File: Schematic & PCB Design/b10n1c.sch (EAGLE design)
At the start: 26 parts, among them U1 nRF8001, Y1 16MHz, Y2 FC-255 32.7680K-A3

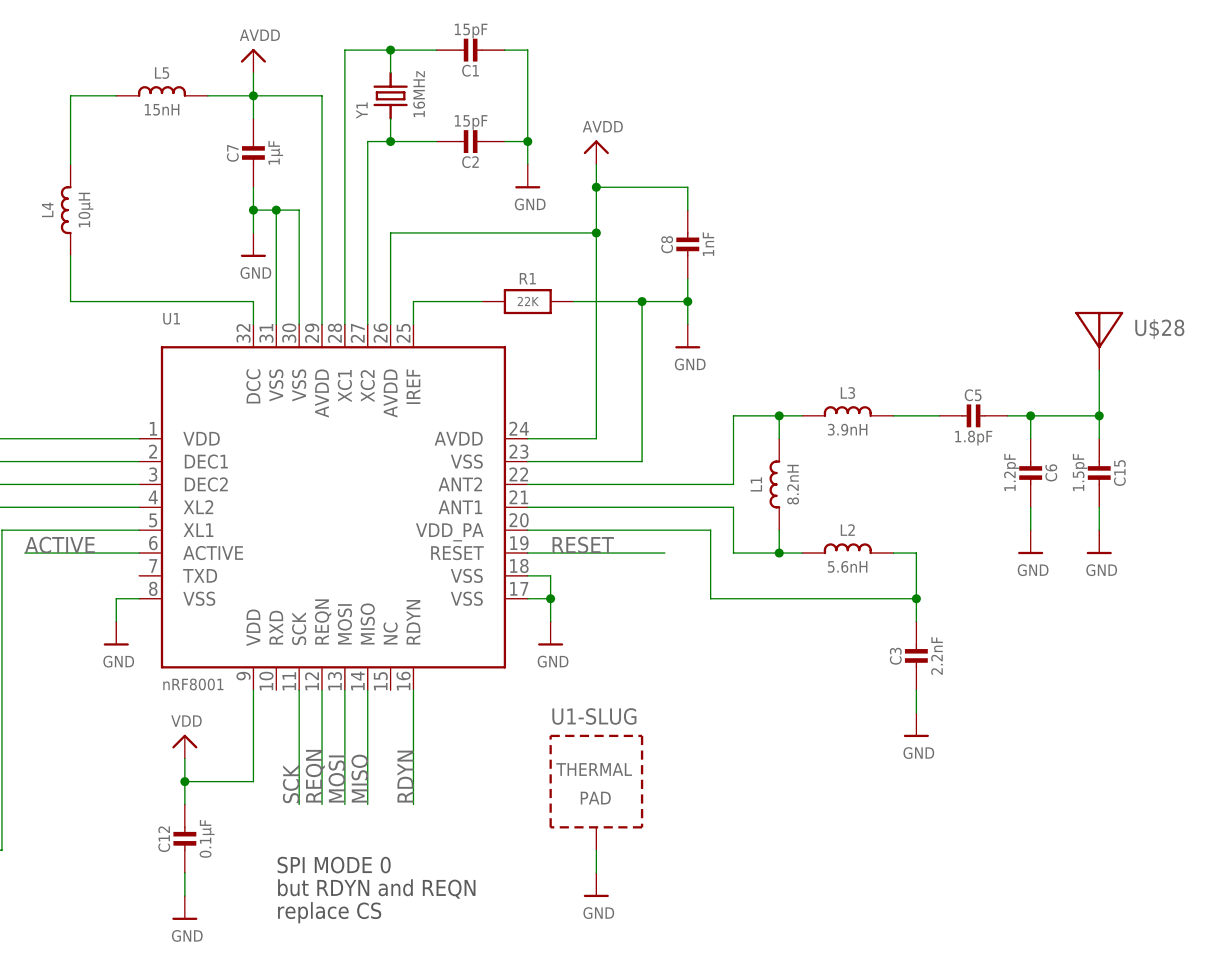
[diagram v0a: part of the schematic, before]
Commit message: Improvement for NRF8001 circuit
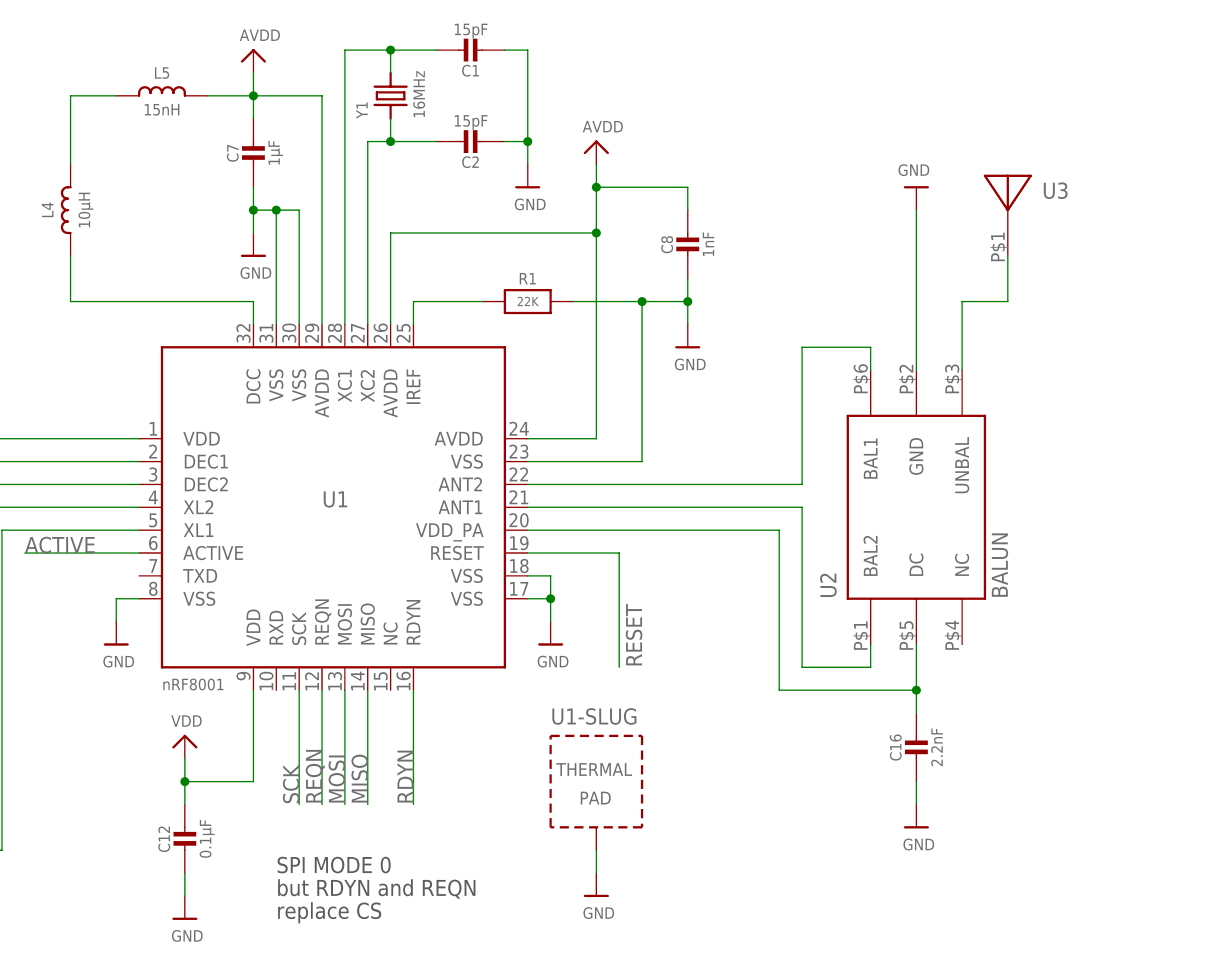
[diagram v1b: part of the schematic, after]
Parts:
- removed C15: 1.5pF, microbuilder:CAP_CERAMIC_0402MP
- removed C3: 2.2nF, microbuilder:CAP_CERAMIC_0402
- removed C5: 1.8pF, microbuilder:CAP_CERAMIC_0402MP
- removed C6: 1.2pF, microbuilder:CAP_CERAMIC_0402MP
- removed L1: 8.2nH, microbuilder:INDUCTOR_0402
- removed L2: 5.6nH, microbuilder:INDUCTOR_0402
- removed L3: 3.9nH, microbuilder:INDUCTOR_0402
- removed U$28: (no value), microbuilder:ANTENNA_PCBNRF8001_1.6MM
- added C16: 2.2nF, microbuilder:CAP_CERAMIC_0402
- added U2: 2450BM14A0002T, baluns:2450BM14A0002T
- added U3: 2450AT18A100, Johanson_antenna:2450AT18A100
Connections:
- removed net N$13: C15.2, C5.1, C6.2, U$28.P$1
- removed net N$2: L1.2, L3.1, U1A.ANT2
- removed net N$3: L1.1, L2.1, U1A.ANT1
- removed net N$4: C3.1, L2.2, U1A.VDD_PA
- removed net N$6: C5.2, L3.2
- new net N$1: C16.1, U1A.VDD_PA, U2.DC
- new net N$14: U1A.ANT1, U2.BAL2
- new net N$15: U1A.ANT2, U2.BAL1
- new net N$16: U2.UNBAL, U3.P$1
- net GND: now also C16.2, U2.GND; no longer C15.1, C3.2, C6.1
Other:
- note added: "BALUN"

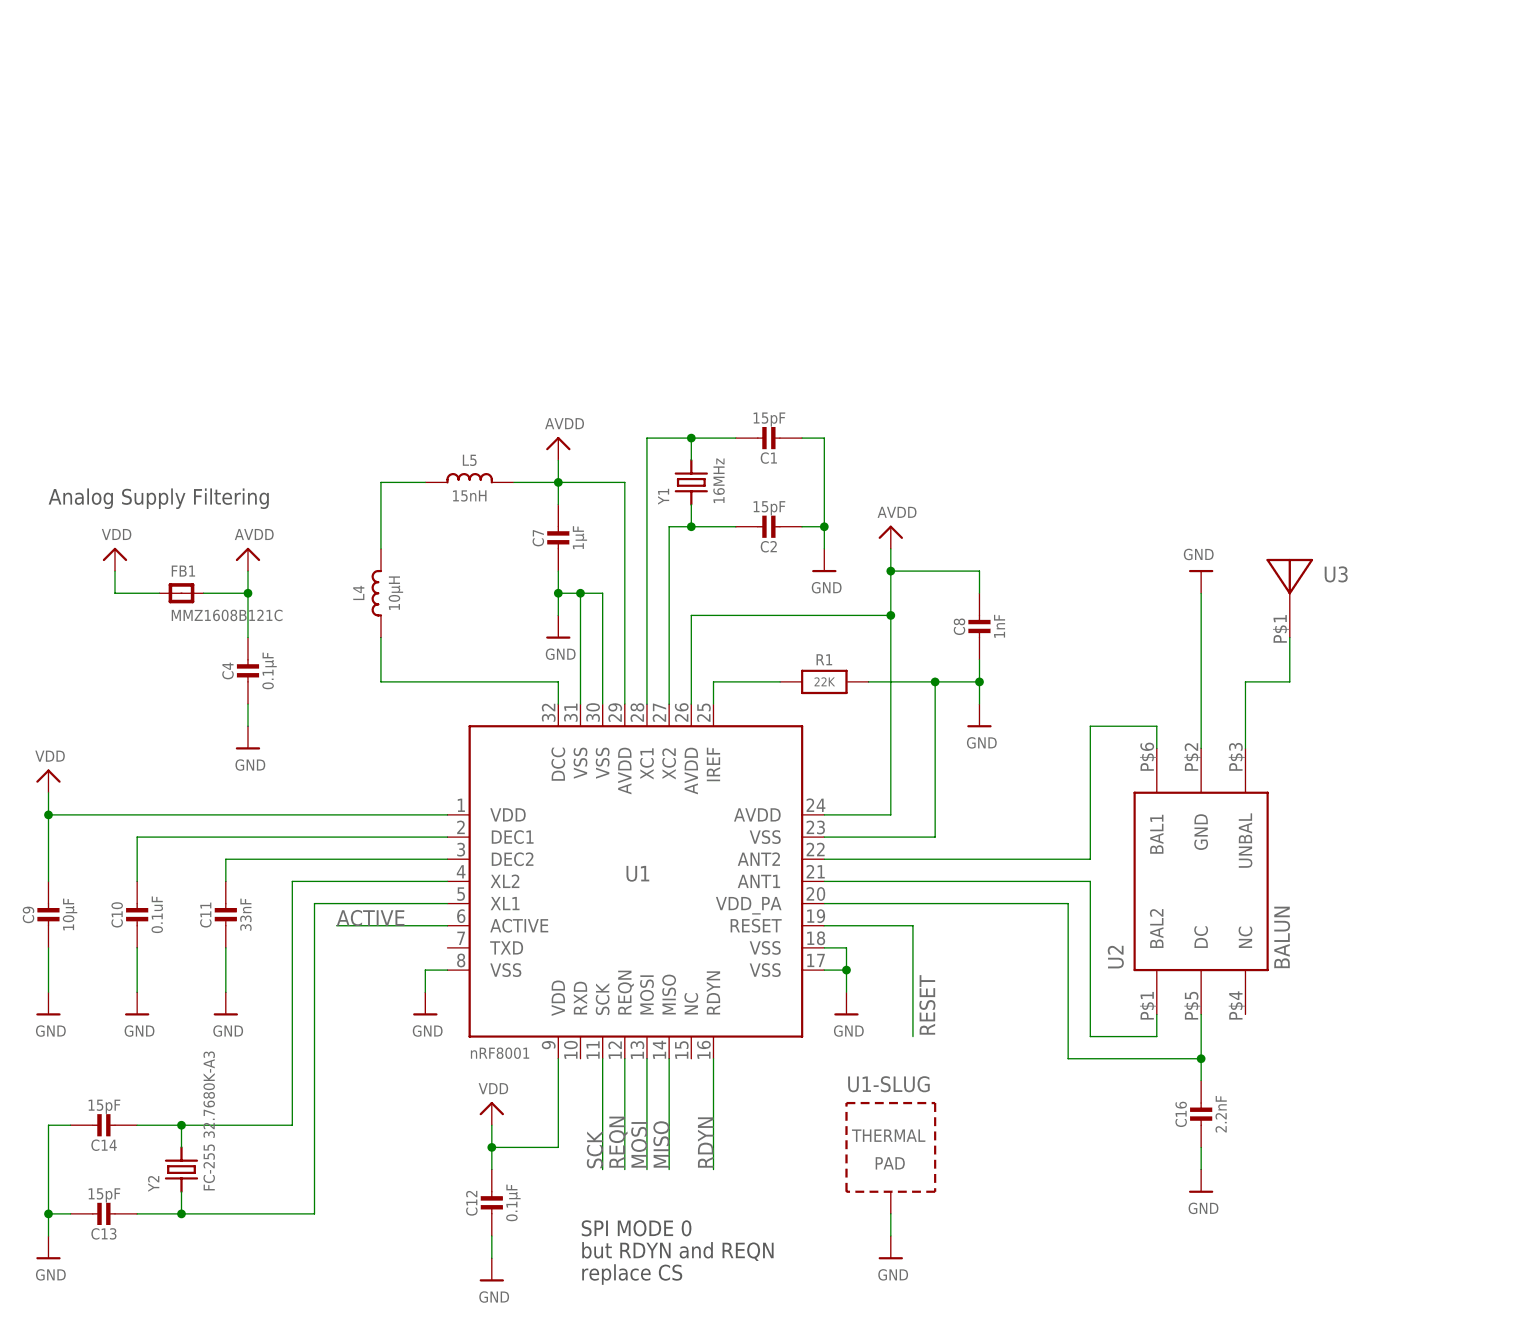
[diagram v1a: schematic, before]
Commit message: NRF8001 schem+layout completed
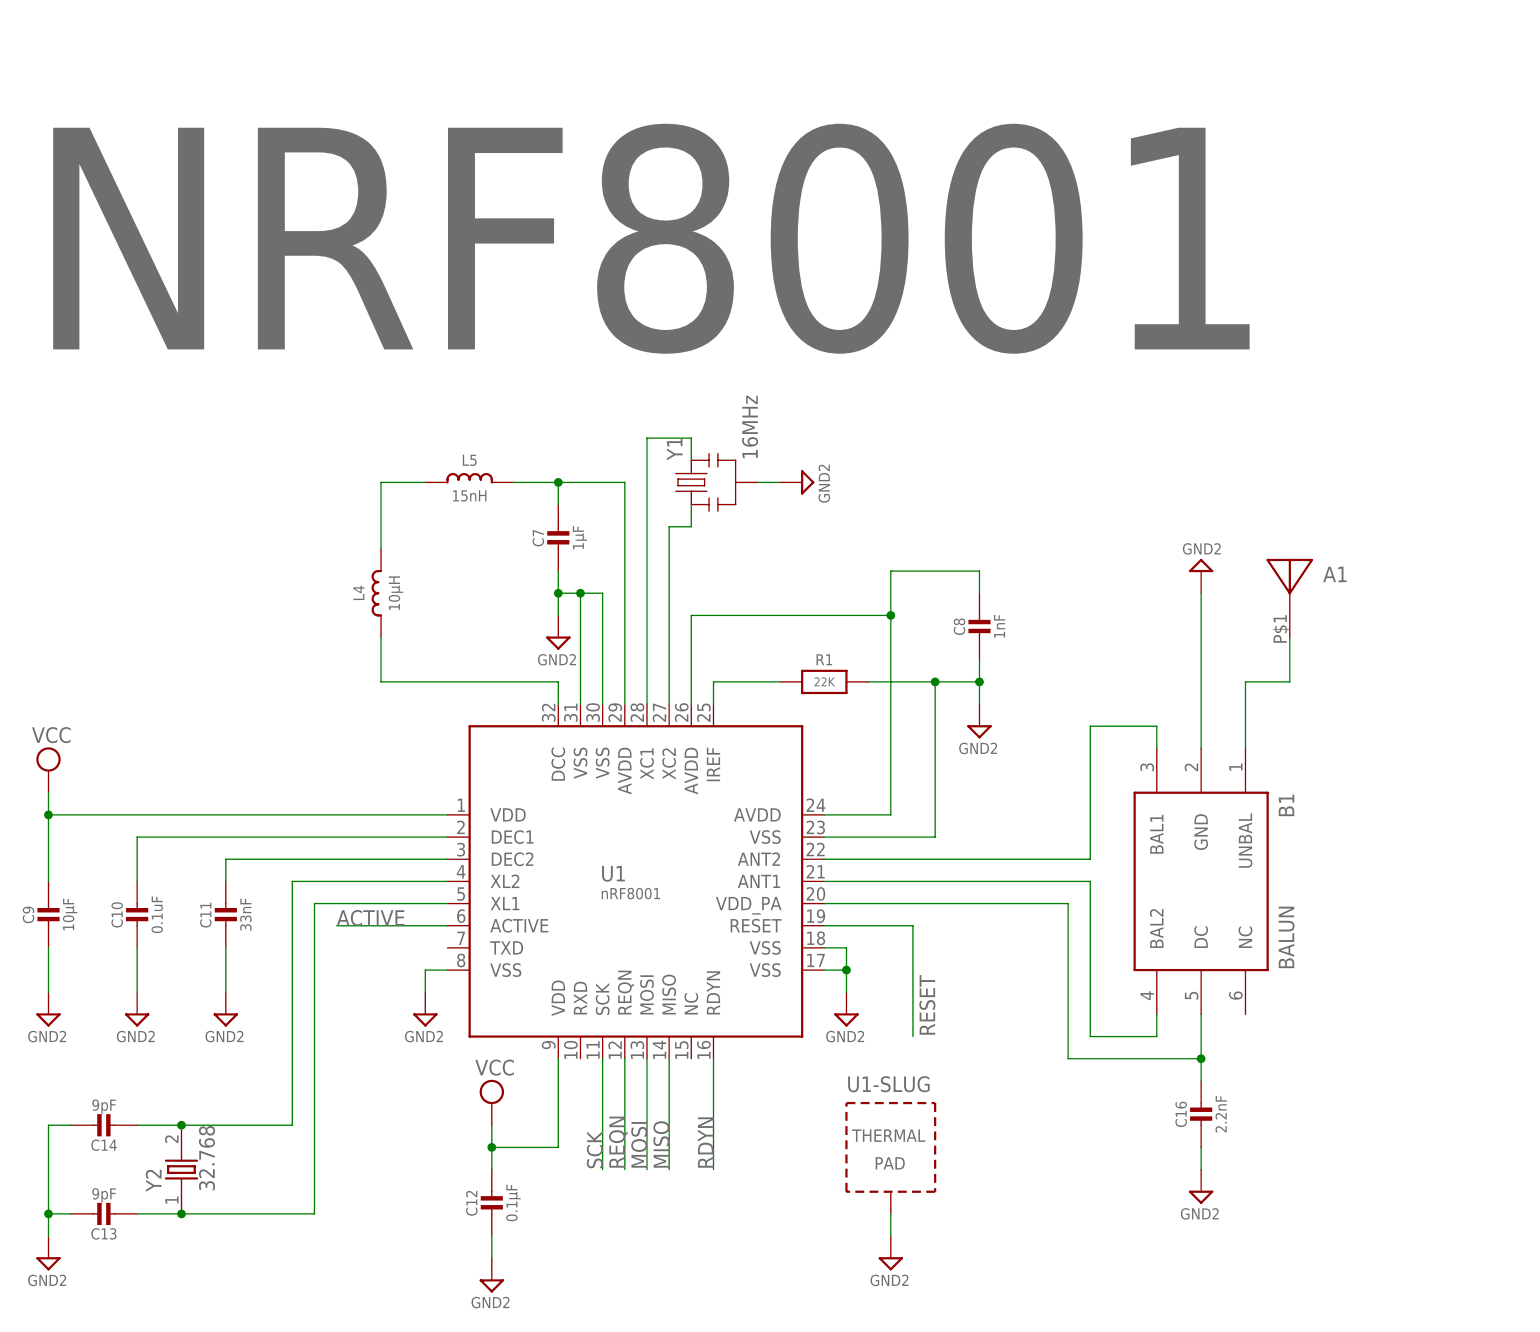
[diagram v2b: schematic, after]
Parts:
- removed C1, C2: 15pF, microbuilder:CAP_CERAMIC0805-NOOUTLINE
- removed C4: 0.1µF, microbuilder:CAP_CERAMIC0805-NOOUTLINE
- removed FB1: MMZ1608B121C, microbuilder:FERRITE0805
- removed U2: 2450BM14A0002T, baluns:2450BM14A0002T
- added B1: 2450BM14A0002T, Johanson_balun:2450BM14A0002T
- C10, C11, C12, C7, C9: device microbuilder:CAP_CERAMIC0805-NOOUTLINE -> microbuilder:CAP_CERAMIC_0402MP
- C13, C14: value 15pF -> 9pF; device microbuilder:CAP_CERAMIC0805-NOOUTLINE -> microbuilder:CAP_CERAMIC_0402MP; DIGIKEY (none) -> 490-5880-1-ND
- C16: device microbuilder:CAP_CERAMIC_0402 -> microbuilder:CAP_CERAMIC_0402MP
- C8: device microbuilder:CAP_CERAMIC_0603 -> microbuilder:CAP_CERAMIC_0402MP
- L4: device microbuilder:INDUCTOR_0603 -> microbuilder:INDUCTOR_0603MP
- L5: device microbuilder:INDUCTOR_0603 -> microbuilder:INDUCTOR_0402MP; DIGIKEY (none) -> 712-1408-1-ND
- R1: device microbuilder:RESISTOR_0805MP -> microbuilder:RESISTOR_0402MP
- Y1: device microbuilder:CRYSTAL2.5X2.0 -> SparkFun-FreqCtrl:RESONATOR16MHZ
- Y2: value FC-255 32.7680K-A3 -> 32.768; device microbuilder:CRYSTAL4.9X1.8 -> Crystal-ABS05-32.768KHZ-9-T:CRYSTAL2PIN
- renumbered U3 to A1
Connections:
- removed net AVDD: C4.1, C7.1, C8.1, FB1.P$2, L5.2, U1A.AVDD@1, U1A.AVDD@2, U1A.AVDD@3
- removed net GND: C1.2, C10.2, C11.2, C12.2, C13.1, C14.1, C16.2, C2.2, C4.2, C7.2, C8.2, C9.2, R1.2, U1-SLUG.TP, U1A.VSS@1, U1A.VSS@2, U1A.VSS@3, U1A.VSS@4, U1A.VSS@5, U1A.VSS@6, U2.GND
- removed net VDD: C12.1, C9.1, FB1.P$1, U1A.VDD@1, U1A.VDD@2
- new net GND2: B1.GND, C10.2, C11.2, C12.2, C13.1, C14.1, C16.2, C7.2, C8.2, C9.2, R1.2, U1-SLUG.TP, U1A.VSS@1, U1A.VSS@2, U1A.VSS@3, U1A.VSS@4, U1A.VSS@5, U1A.VSS@6, Y1.2
- new net N$2: C7.1, L5.2, U1A.AVDD@3
- new net N$3: C8.1, U1A.AVDD@1, U1A.AVDD@2
- new net VCC: C12.1, C9.1, U1A.VDD@1, U1A.VDD@2
- net N$1: now also B1.DC; no longer U2.DC
- net N$10: no longer C2.1
- net N$14: now also B1.BAL2; no longer U2.BAL2
- net N$15: now also B1.BAL1; no longer U2.BAL1
- net N$16: now also B1.UNBAL; no longer U2.UNBAL
- net N$9: now also Y1.3; no longer C1.1, Y1.2
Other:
- note added: "NRF8001"
- note removed: "Analog Supply Filtering"
- note removed: "SPI MODE 0"
- note removed: "but RDYN and REQN"
- note removed: "replace CS"

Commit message: ATMEGA328 & PN532 circuit added to b10n1c schamtic
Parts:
- added C1, C15, C19, C2, C21, C22, C25, C27, C28: 0.1µF, microbuilder:CAP_CERAMIC_0402MP
- added C17, C18: 33pF, microbuilder:CAP_CERAMIC_0402MP
- added C20: 1000pF, microbuilder:CAP_CERAMIC_0402MP
- added C23, C24, C26, C29: 10µF, microbuilder:CAP_CERAMIC_0402MP
- added C3, C4: 22pF, microbuilder:CAP_CERAMIC_0402MP
- added C30, C31: 220pF, microbuilder:CAP_CERAMIC_0402MP
- added C5, C6: 100pF, microbuilder:CAP_CERAMIC_0402MP
- added FB1, FB2: (no value), microbuilder:FERRITE_0402MP
- added L1, L3: 560nH, microbuilder:INDUCTOR_0402MP
- added R2: 10K, microbuilder:RESISTOR_0402MP
- added R3: 1.0K, microbuilder:RESISTOR_0402MP
- added R4: 1.69K, microbuilder:RESISTOR_0402MP
- added R5, R6: 1.5, microbuilder:RESISTOR_0402MP
- added TP4: TX2_PRE, microbuilder:TESTPOINTPAD
- added TP5: TX1_PRE, microbuilder:TESTPOINTPAD
- added U2: ATMEGA328P-MU, Smartprj:ATMEGAXX8-MU
- added U3: PN532, microbuilder:PN532
- added Y3: 8MHZ, SparkFun-FreqCtrl:RESONATOR8MHZ
- added Y4: 27.12MHz, microbuilder:CRYSTALTHIN
- Y2: DIGIKEY (none) -> 490-1198-1-ND
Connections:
- removed net RDYN: U1A.RDYN
- removed net REQN: U1A.REQN
- new net +3V3: C1.P$1, R2.2, U2.AVCC, U2.VCC@1, U2.VCC@2
- new net ADC2: U2.PC2(ADC2)
- new net ADC3: U2.PC3(ADC3)
- new net ADC6: U2.ADC6
- new net ADC7: U2.ADC7
- new net AREF: C2.P$1, U2.AREF
- new net AUX1: U3.AUX1
- new net AUX2: U3.AUX2
- new net GND: C1.P$2, C15.P$2, C17.P$2, C18.P$2, C19.P$2, C2.P$2, C21.P$2, C22.P$2, C23.P$2, C24.P$2, C25.P$2, C26.P$1, C27.P$2, C28.P$2, C29.P$2, C30.P$2, C31.P$1, C5.P$2, C6.P$1, U2.AGND, U2.GND@1, U2.GND@2, U3.AGND, U3.DGND, U3.TESTEN, U3.TGND1, U3.TGND2, U3.THERMAL, Y3.2
- new net IO2: U2.PD2(INT0)
- new net IO3: U2.PD3(INT1)
- new net IO4: U2.PD4(XCK/T0)
- new net IO5: U2.PD5(T1)
- new net IO6: U2.PD6(AIN0)
- new net IO7: U2.PD7(AIN1)
- new net IO8: U2.PB0(ICP)
- new net IO9: U2.PB1(OC1A)
- new net IRQ: U3.IRQ
- new net N$13: L3.2, U3.TX1
- new net N$17: L1.2, U3.TX2
- new net N$18: C3.P$2, C30.P$1, L3.1
- new net N$19: C17.P$1, U3.XTAL1, Y4.1
- new net N$20: C18.P$1, U3.XTAL2, Y4.2
- new net N$21: C19.P$1, R3.2, U3.VMID
- new net N$24: C20.P$2, R3.1, U3.RX
- new net N$25: C20.P$1, R4.1
- new net N$26: C31.P$2, C4.P$1, L1.1, R4.2
- new net N$27: R5.1, TP5.P$1
- new net N$28: R6.2, TP4.P$1
- new net N$29: C15.P$1, C29.P$1, FB2.P$2, U3.AVDD
- new net N$30: C24.P$1, C27.P$1, FB1.P$2, U3.TVDD
- new net N$4: U2.PB6(XTAL1/TOSC1), Y3.3
- new net N$6: U2.PB7(XTAL2/TOSC2), Y3.1
- new net P31: U3.P31
- new net P32: U3.P32
- new net P33: U3.P33
- new net P34/SIC_CLK: U3.P34/SIC_CLK
- new net P35: U3.P35
- new net RDY: U1A.RDYN, U2.PC1(ADC1)
- new net REQ: U1A.REQN, U2.PB2(SS/OC1B)
- new net RST: U1A.RESET, U2.PC0(ADC0)
- new net RSTOUT_N: U3.RSTOUT_N
- new net RSTPD_N: U3.RSTPD_N
- new net RX: U2.PD0(RXD)
- new net SCL: U2.PC5(ADC5/SCL), U3.NSS/P50_SCL/HSU_RX
- new net SDA: U2.PC4(ADC4/SDA), U3.MOSI/SDA/HSU_TX
- new net SEL0: U3.I0
- new net SEL1: U3.I1
- new net SIGIN: U3.SIGIN
- new net SIGOUT: U3.SIGOUT
- new net TX: U2.PD1(TXD)
- new net TX1_ANTENNA: C3.P$1, C5.P$1, R5.2
- new net TX2_ANTENNA: C4.P$2, C6.P$2, R6.1
- new net VDD: C21.P$1, C22.P$1, C23.P$1, C25.P$1, C26.P$2, C28.P$1, FB1.P$1, FB2.P$1, U3.DVDD, U3.PVDD, U3.SVDD, U3.VBAT
- net GND2: now also C10.P$2, C11.P$2, C12.P$2, C13.P$1, C14.P$1, C16.P$2, C7.P$2, C8.P$2, C9.P$2; no longer C10.2, C11.2, C12.2, C13.1, C14.1, C16.2, C7.2, C8.2, C9.2
- net MISO: now also U2.PB4(MISO)
- net MOSI: now also U2.PB3(MOSI/OC2)
- net N$1: now also C16.P$1; no longer C16.1
- net N$2: now also C7.P$1; no longer C7.1
- net N$22: now also C14.P$2; no longer C14.2
- net N$23: now also C13.P$2; no longer C13.2
- net N$3: now also C8.P$1; no longer C8.1
- net N$7: now also C11.P$1; no longer C11.1
- net N$8: now also C10.P$1; no longer C10.1
- net RESET: now also R2.1, U2.PC6(/RESET); no longer U1A.RESET
- net SCK: now also U2.PB5(SCK)
- net VCC: now also C12.P$1, C9.P$1; no longer C12.1, C9.1
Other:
- note added: "ADC0"
- note added: "ADC1"
- note added: "ADC2"
- note added: "ADC3"
- note added: "ADC4"
- note added: "ADC5"
- note added: "ANTENNA MATCHING CIRCUIT"
- note added: "For 887-1329-1-ND"
- note added: "For 887-1424-1-ND"
- note added: "IO10"
- note added: "IO11"
- note added: "IO12"
- note added: "IO13"
- note added: "IO8"
- note added: "IO9"
- note added: "MEGA328"
- note added: "PN532"
- note added: "nRF8001"
- note added: "use 16 or 22pF caps"
- note added: "use 33pF Caps"
- note removed: "NRF8001"
- moved on the sheet: C10, C11, C13, C14, C16, C9, U1-SLUG, Y2
